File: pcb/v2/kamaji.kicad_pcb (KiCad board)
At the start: 2 copper layers, 100 x 100 mm, 70 parts, among them J1 RJ10, J2 RJ10, J3 RJ10, J4 RJ10, J5 RJ10, J6 RJ10, J7 USB_B, J8 USB_A, Q1 2N3904, Q2 IRL540N, Q3 IRL540N, SW1 SW_Push, SW2 SW_Push, SW3 SW_Push, U1 ATMEGA32U4-AU, Y1 16MHz

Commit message: move a couple components
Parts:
- removed the REF** at (54.0, 57.0)
- removed the REF** at (146.0, 57.0)
- removed the REF** at (54.0, 143.0)
- removed the REF** at (146.0, 143.0)
- removed the VIA** at (79.5, 100.0)
- added REF**: 1pin, kamaji:Drill_Hole_M3, F.Cu at (146.0, 57.0)
- added REF**: 1pin, kamaji:Drill_Hole_M3, F.Cu at (54.0, 57.0)
- added REF**: 1pin, kamaji:Drill_Hole_M3, F.Cu at (54.0, 143.0)
- added REF**: 1pin, kamaji:Drill_Hole_M3, F.Cu at (146.0, 143.0)
- added VIA**: Via_0.8mm, kamaji:Via_0.8mm, F.Cu at (70.0, 80.5)
- added VIA**: Via_0.8mm, kamaji:Via_0.8mm, F.Cu at (93.5, 118.5)
- added VIA**: Via_0.8mm, kamaji:Via_0.8mm, F.Cu at (121.0, 73.5)
- added VIA**: Via_0.8mm, kamaji:Via_0.8mm, F.Cu at (101.0, 78.5)
- added VIA**: Via_0.8mm, kamaji:Via_0.8mm, F.Cu at (73.0, 106.0)
- moved JP2 11.5 mm to (79.8, 100.2)
- moved JP3 11.5 mm to (83.5, 100.2)
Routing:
- net /Boost Converter/BOOST_VOUT: track 24.8 -> 37.2 mm
- net VCC: track 267.0 -> 276.8 mm
- net Net-(JP2-Pad2): track 7.43 -> 15.6 mm

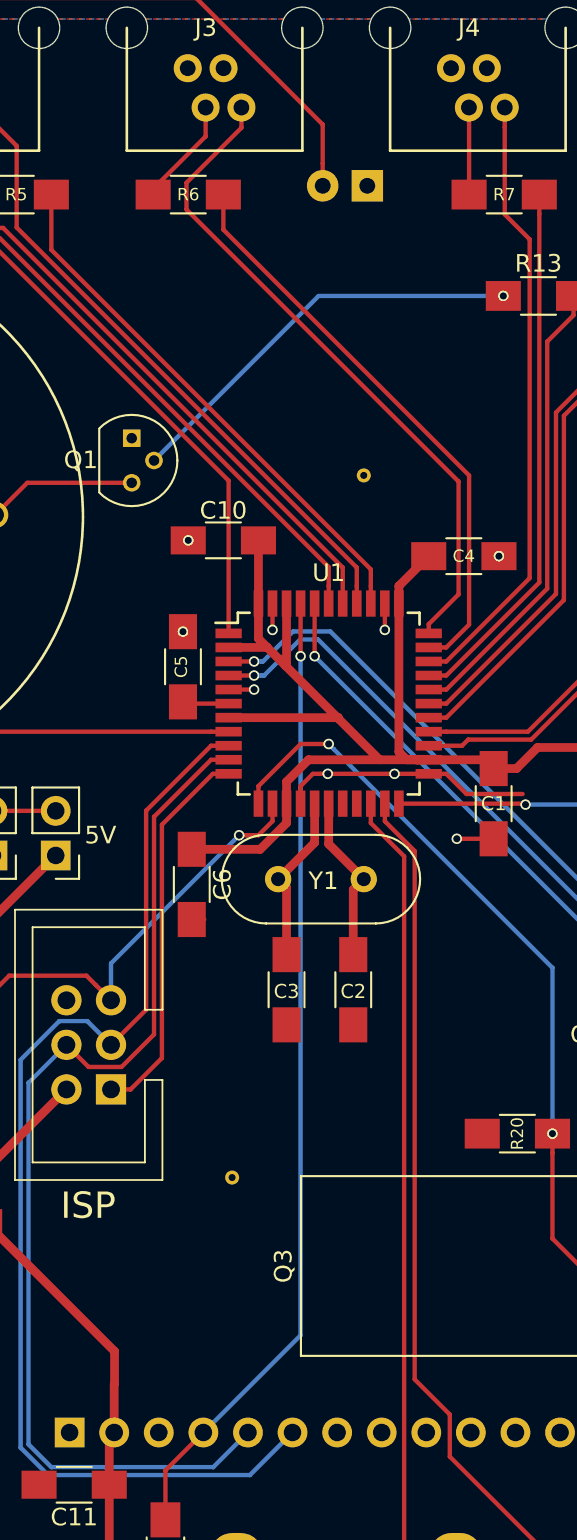
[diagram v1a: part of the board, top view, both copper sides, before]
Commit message: pull HWB down
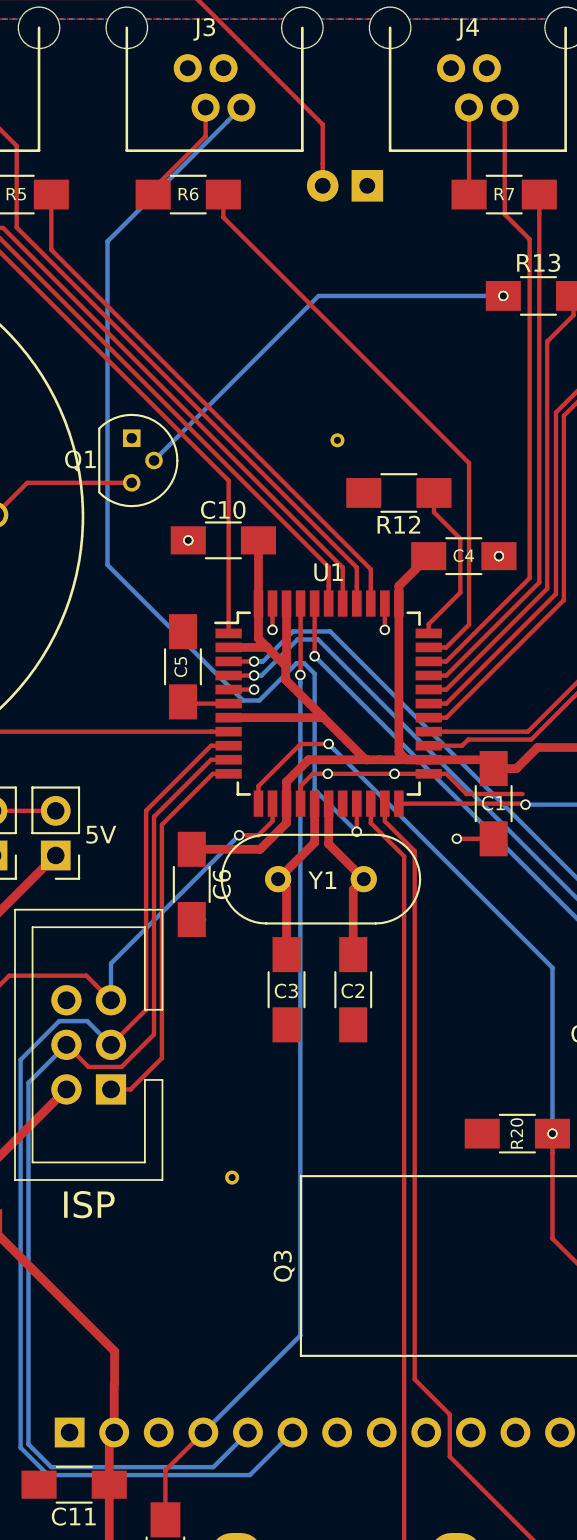
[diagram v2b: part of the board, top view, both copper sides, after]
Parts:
- added R12: 10K, Resistors_SMD:R_1206_HandSoldering, F.Cu at (103.0, 79.5)
- moved VIA** 2.50 mm to (99.5, 76.5)
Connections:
- U1 pad 19: (no net) -> /PBTN3
- U1 pad 33: /PBTN3 -> Net-(R12-Pad1)
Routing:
- net /PBTN3: track 38.4 -> 56.9 mm, vias 0 -> 1
- net Net-(R12-Pad1): track 0.00 -> 9.37 mm
- net VCC: track 276.8 -> 275.6 mm
- net GND: vias 12 -> 11

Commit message: bump the PCB version
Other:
- board text added: "Kamaji 2.2"
- board text removed: "Kamaji 2.1"
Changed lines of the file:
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@@
     (links 166)
     (no_connects 0)
-    (area 49.924999 49.924999 150.075001 150.075001)
+    (area 46.224999 46.55 152.775001 150.075001)
     (thickness 1.6)
     (drawings 16)
@@
     )
   )
-  (gr_text "Kamaji 2.1" (at 123 61) (layer B.SilkS)
+  (gr_text "Kamaji 2.2" (at 123 61) (layer B.SilkS)
     (effects (font (size 2 2) (thickness 0.25)) (justify mirror))
   )

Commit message: simplify the PCB a bit
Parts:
- removed R14: 0, Resistors_SMD:R_1206_HandSoldering
- removed R25, R26: 10K, Resistors_SMD:R_1206_HandSoldering
- added VIA**: Via_0.8mm, kamaji:Via_0.8mm, F.Cu at (95.5, 93.7)
- added VIA**: Via_0.8mm, kamaji:Via_0.8mm, F.Cu at (86.7, 100.0)
- moved R8 10.9 mm to (93.8, 129.9), turned to 180 degrees
- moved C11 0.32 mm to (84.8, 135.9)
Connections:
- DS1 pad 15: Net-(DS1-Pad15) -> GND
- RV2 pad 3: Net-(R14-Pad1) -> Net-(JP2-Pad2)
- VIA** pad 1: (no net) -> GND (x5)
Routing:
- net Net-(JP2-Pad2): track 15.6 -> 22.0 mm
- net Net-(DS1-Pad15): track 5.27 -> 0.00 mm
- net Net-(R14-Pad1): track 4.42 -> 0.00 mm
- net /LCD_RST: track 62.2 -> 58.3 mm
- net /LCD_CS: track 55.4 -> 52.6 mm
- net VCC: track 275.6 -> 273.0 mm
- net /SCK: track 66.3 -> 66.8 mm

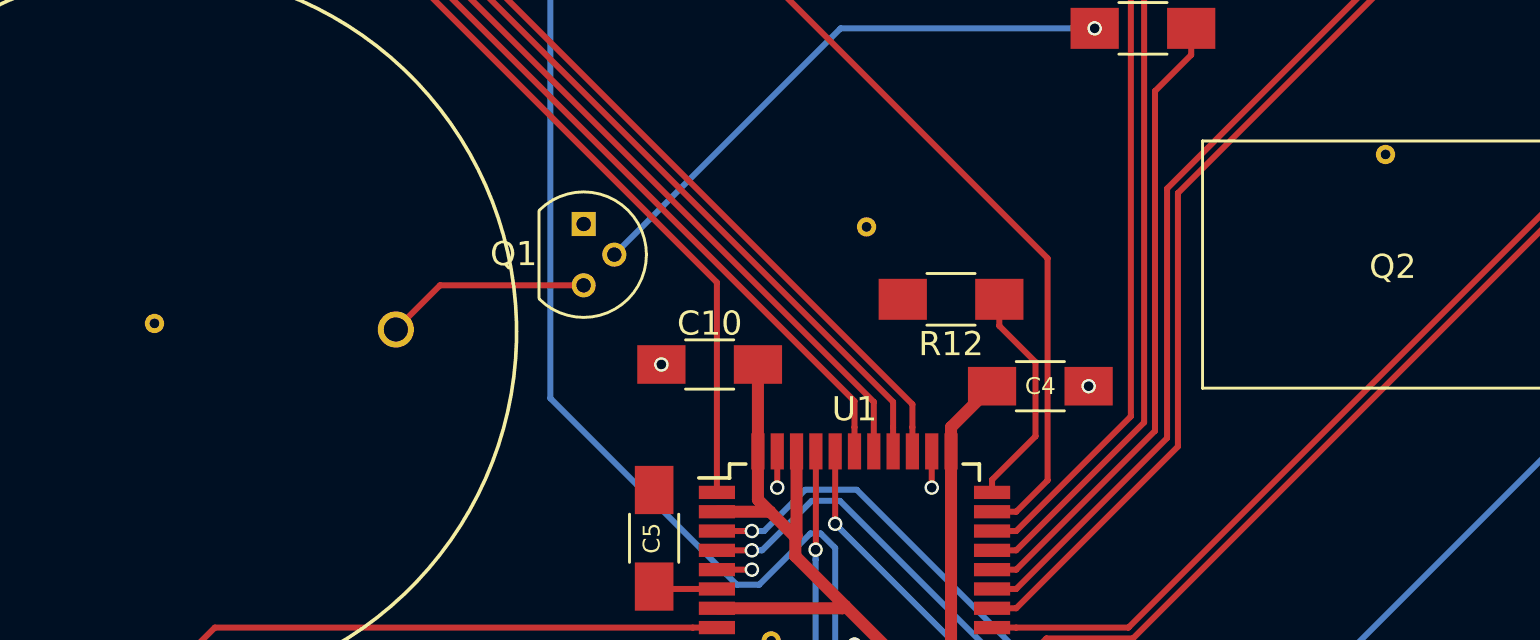
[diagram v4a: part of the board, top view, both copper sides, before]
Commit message: move a couple tracks and vias
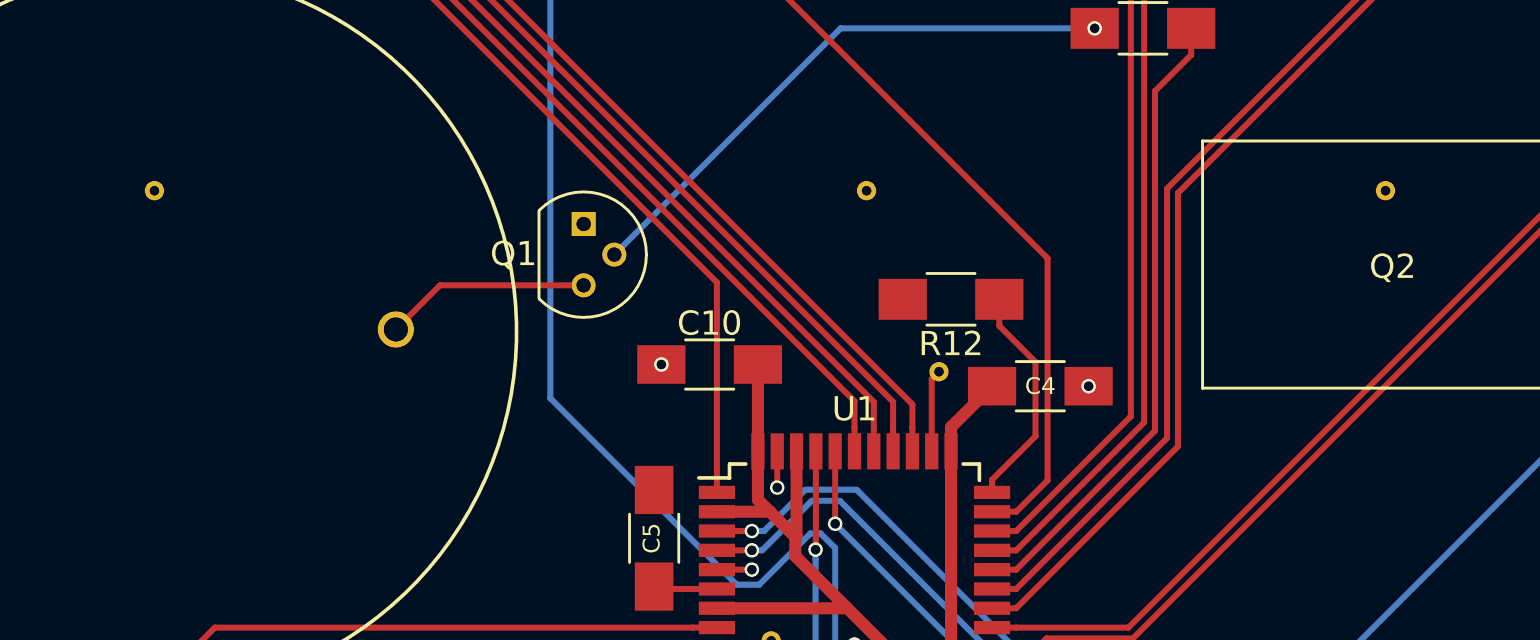
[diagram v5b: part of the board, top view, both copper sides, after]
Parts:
- added VIA**: Via_0.8mm, kamaji:Via_0.8mm, F.Cu at (102.5, 82.5)
- moved VIA** 5.50 mm to (70.0, 75.0)
- moved VIA** 1.50 mm to (121.0, 75.0)
- moved VIA** 1.50 mm to (99.5, 75.0)
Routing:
- net GND: track 25.3 -> 27.3 mm, vias 11 -> 10
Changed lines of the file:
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@@
     (tracks 395)
     (zones 0)
-    (modules 74)
+    (modules 75)
     (nets 57)
   )
@@
   )
   (module kamaji:Via_0.8mm (layer F.Cu)
+    (at 102.5 82.5)
+    (fp_text reference VIA** (at 0 1.5) (layer F.SilkS) hide
+      (effects (font (size 1 1) (thickness 0.15)))
+    )
+    (fp_text value Via_0.8mm (at 0 -1.5) (layer F.Fab) hide
+      (effects (font (size 1 1) (thickness 0.15)))
+    )
+    (pad 1 thru_hole circle (at 0 0) (size 0.8 0.8) (drill 0.4) (layers *.Cu)
+      (net 47 GND) (zone_connect 2))
+  )
+  (module kamaji:Via_0.8mm (layer F.Cu)
     (at 95.55 93.65)
     (fp_text reference VIA** (at 0 1.5) (layer F.SilkS) hide
@@
   )
   (module kamaji:Via_0.8mm (layer F.Cu)
-    (at 70 80.5)
+    (at 70 75)
     (fp_text reference VIA** (at 0 1.5) (layer F.SilkS) hide
       (effects (font (size 1 1) (thickness 0.15)))
@@
   )
   (module kamaji:Via_0.8mm (layer F.Cu)
-    (at 121 73.5)
+    (at 121 75)
     (fp_text reference VIA** (at 0 1.5) (layer F.SilkS) hide
       (effects (font (size 1 1) (thickness 0.15)))
@@
   )
   (module kamaji:Via_0.8mm (layer F.Cu)
-    (at 99.5 76.5)
+    (at 99.5 75)
     (fp_text reference VIA** (at 0 1.5) (layer F.SilkS) hide
       (effects (font (size 1 1) (thickness 0.15)))
@@
   (segment (start 104.7 93.9) (end 106.6 93.9) (width 0.25) (layer F.Cu) (net 46))
   (segment (start 139.5 63.6) (end 139.5 62.5) (width 0.25) (layer F.Cu) (net 46))
+  (segment (start 102.2 85.8) (end 102.2 82.8) (width 0.25) (layer F.Cu) (net 47))
+  (segment (start 102.2 82.8) (end 102.5 82.5) (width 0.25) (layer F.Cu) (net 47))
   (segment (start 93.3 90.7) (end 94.749985 90.7) (width 0.25) (layer F.Cu) (net 47))
   (via (at 94.75 90.700015) (size 0.6) (drill 0.4) (layers F.Cu B.Cu) (net 47))
@@
   (segment (start 108.4 99.2) (end 106.3 99.2) (width 0.25) (layer F.Cu) (net 47))
   (via (at 106.3 99.2) (size 0.6) (drill 0.4) (layers F.Cu B.Cu) (net 47))
-  (segment (start 102.2 85.8) (end 102.2 87.299998) (width 0.25) (layer F.Cu) (net 47))
-  (via (at 102.2 87.299998) (size 0.6) (drill 0.4) (layers F.Cu B.Cu) (net 47))
   (segment (start 95.8 85.8) (end 95.8 87.3) (width 0.25) (layer F.Cu) (net 47))
   (via (at 95.8 87.3) (size 0.6) (drill 0.4) (layers F.Cu B.Cu) (net 47))
